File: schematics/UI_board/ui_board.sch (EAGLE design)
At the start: 119 parts, among them IC1 74HCT00N, IC10 74HCT32N, IC11 74HCT14N, IC12 74HCT14N, IC13 74HCT393N, IC2 74HCT151N, IC3 74HCT32N, IC4 74HCT74N, IC5 74HCT04N, IC6 74HCT32N, IC8 74HCT373N, IC9 74HCT32N

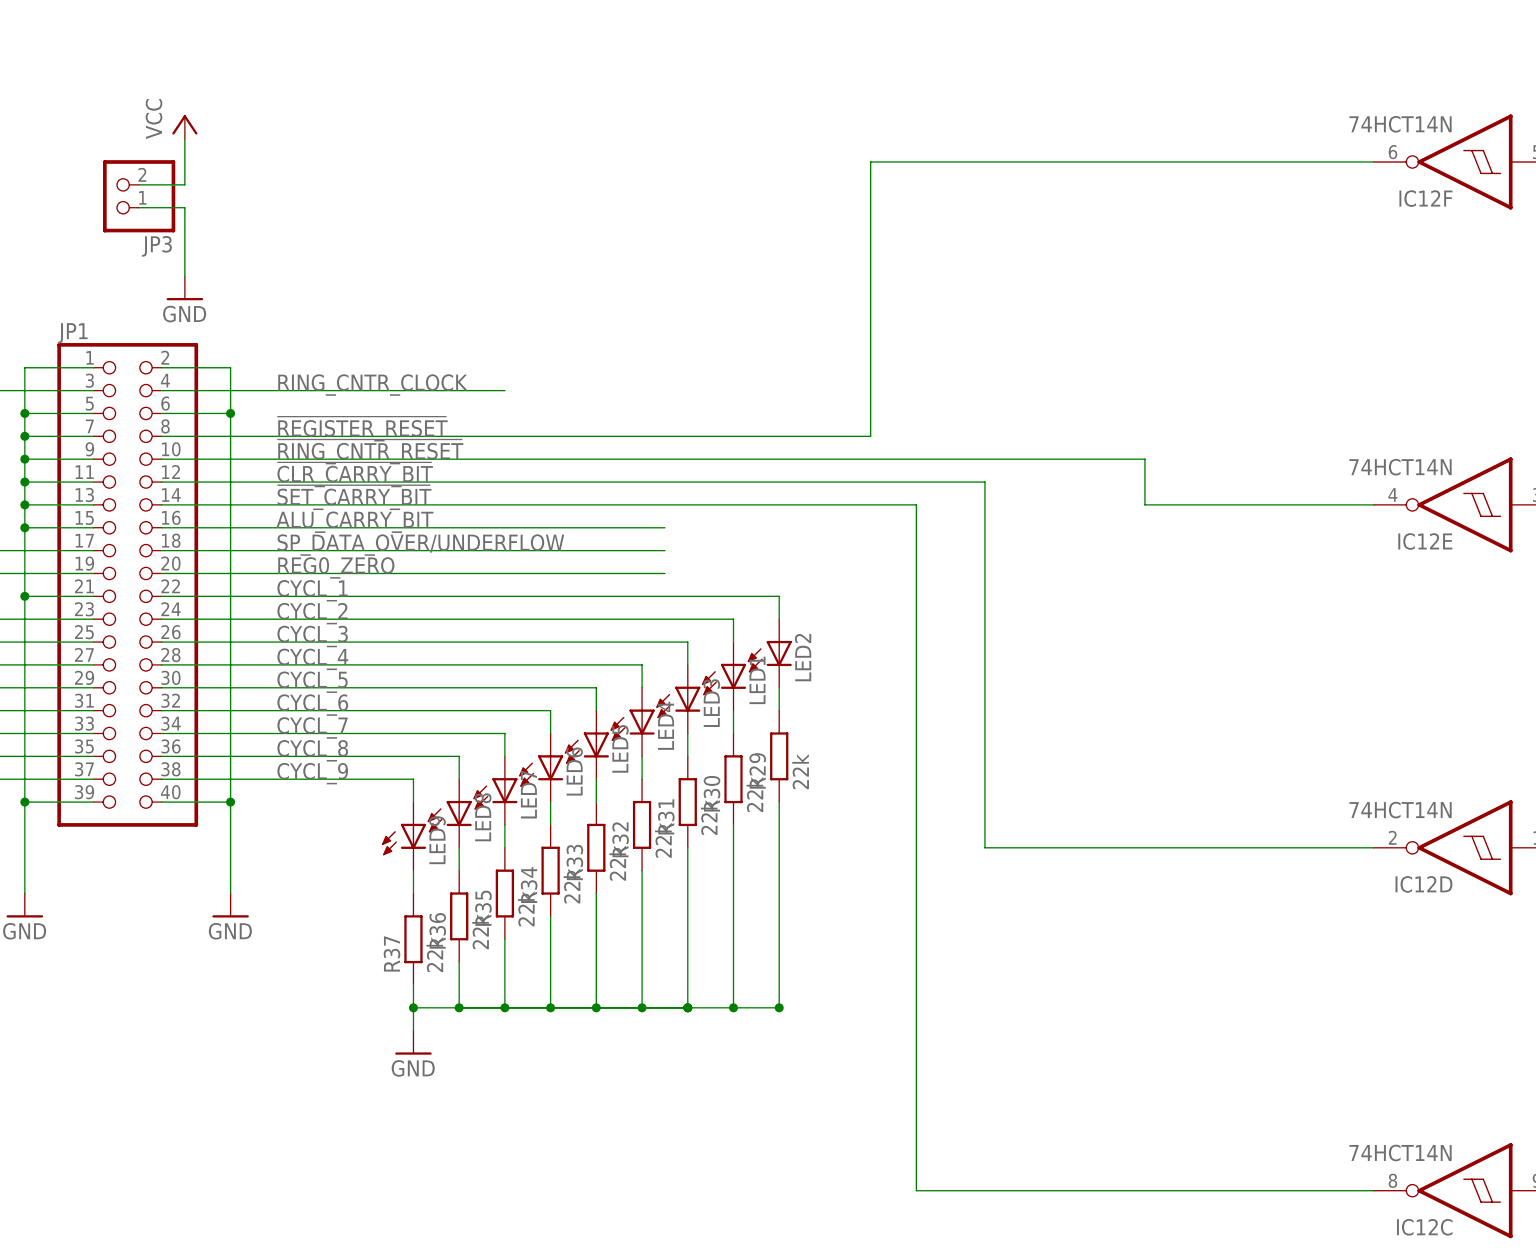
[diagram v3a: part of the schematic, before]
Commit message: got rid of two cycles! finetuning next
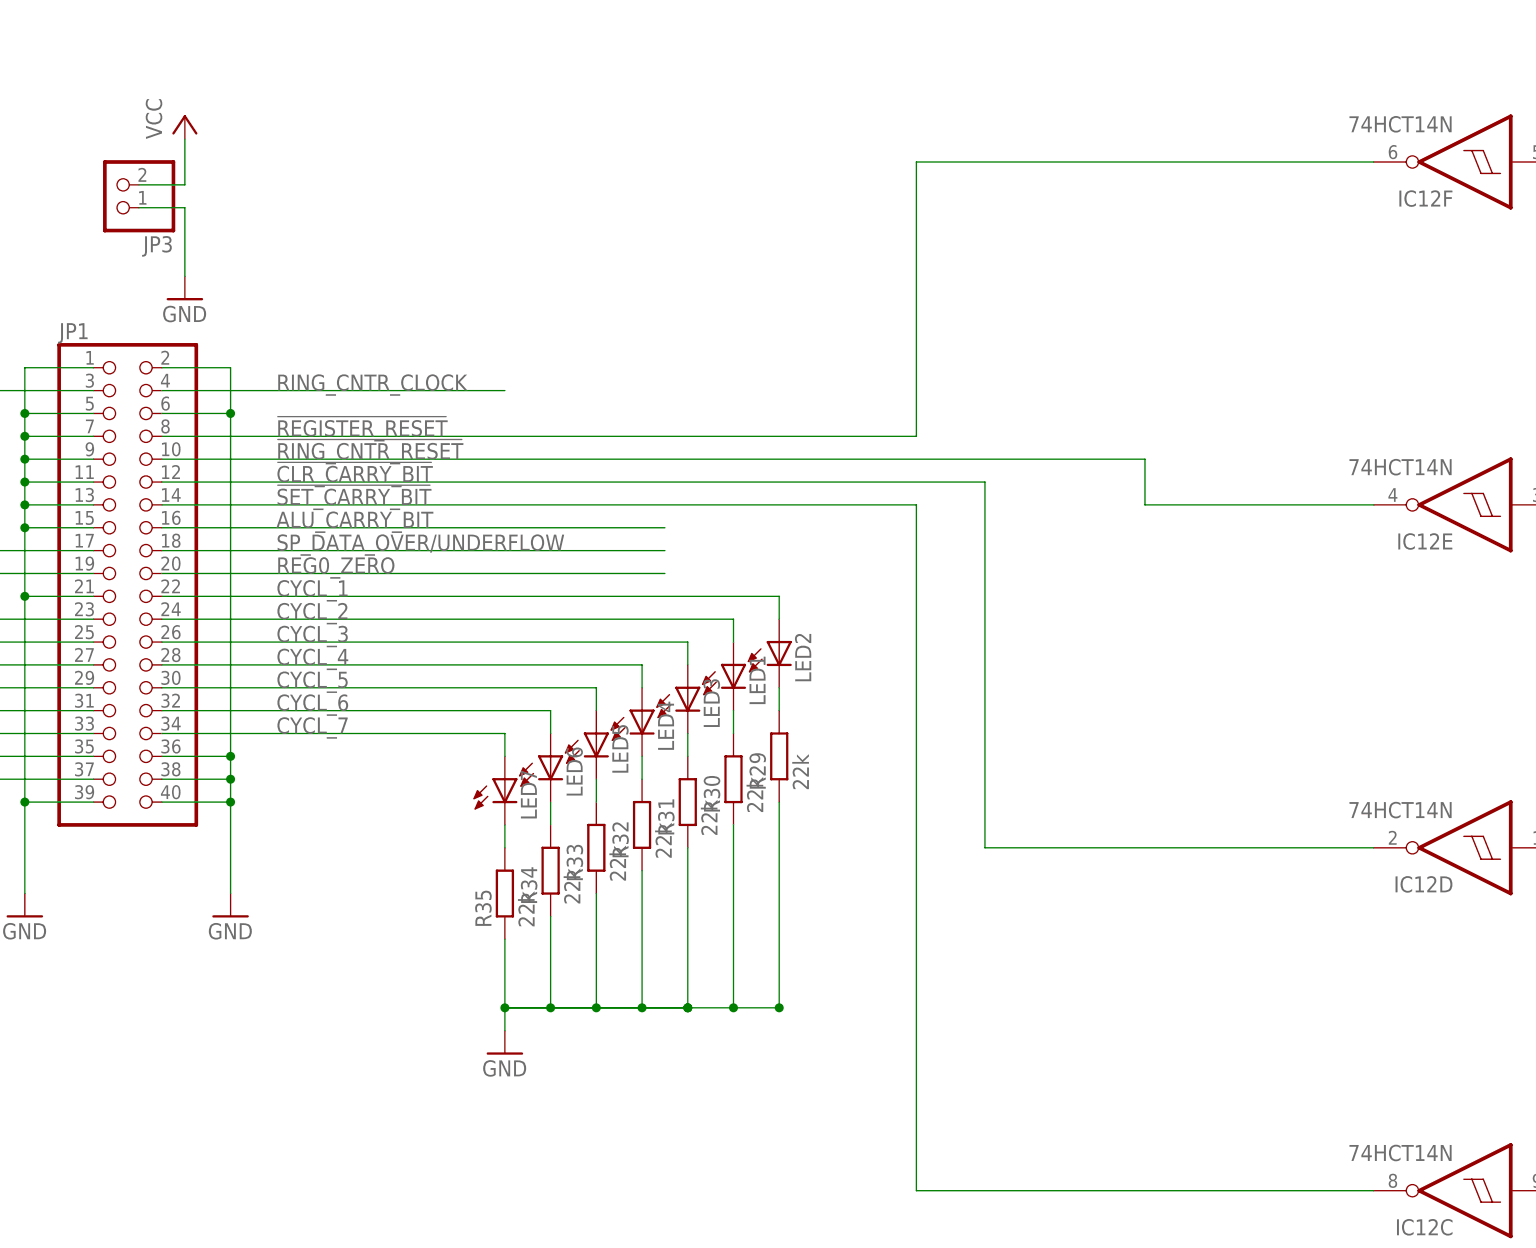
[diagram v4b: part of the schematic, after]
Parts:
- removed LED8, LED9: (no value), led:LED3MM
- removed R36, R37: 22k, rcl:R-EU_R1206
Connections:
- removed net CYCL_8: JP1.36, LED8.A
- removed net CYCL_9: JP1.38, LED9.A
- removed net N$67: LED8.C, R36.2
- removed net N$68: LED9.C, R37.2
- net GND: now also JP1.36, JP1.38; no longer R36.1, R37.1
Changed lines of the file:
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@@
 <part name="LED6" library="led" deviceset="LED" device="3MM"/>
 <part name="LED7" library="led" deviceset="LED" device="3MM"/>
-<part name="LED8" library="led" deviceset="LED" device="3MM"/>
-<part name="LED9" library="led" deviceset="LED" device="3MM"/>
 <part name="R29" library="rcl" deviceset="R-EU_" device="R1206" value="22k"/>
 <part name="R30" library="rcl" deviceset="R-EU_" device="R1206" value="22k"/>
@@
 <part name="R34" library="rcl" deviceset="R-EU_" device="R1206" value="22k"/>
 <part name="R35" library="rcl" deviceset="R-EU_" device="R1206" value="22k"/>
-<part name="R36" library="rcl" deviceset="R-EU_" device="R1206" value="22k"/>
-<part name="R37" library="rcl" deviceset="R-EU_" device="R1206" value="22k"/>
 <part name="GND32" library="supply1" deviceset="GND" device=""/>
 <part name="LED10" library="led" deviceset="LED" device="3MM"/>
@@
 <instance part="LED6" gate="G$1" x="58.42" y="40.64"/>
 <instance part="LED7" gate="G$1" x="53.34" y="38.1"/>
-<instance part="LED8" gate="G$1" x="48.26" y="35.56"/>
-<instance part="LED9" gate="G$1" x="43.18" y="33.02"/>
 <instance part="R29" gate="G$1" x="83.82" y="40.64" rot="R90"/>
 <instance part="R30" gate="G$1" x="78.74" y="38.1" rot="R90"/>
@@
 <instance part="R34" gate="G$1" x="58.42" y="27.94" rot="R90"/>
 <instance part="R35" gate="G$1" x="53.34" y="25.4" rot="R90"/>
-<instance part="R36" gate="G$1" x="48.26" y="22.86" rot="R90"/>
-<instance part="R37" gate="G$1" x="43.18" y="20.32" rot="R90"/>
-<instance part="GND32" gate="1" x="43.18" y="7.62"/>
+<instance part="GND32" gate="1" x="53.34" y="7.62"/>
 <instance part="LED10" gate="G$1" x="-66.04" y="50.8" rot="MR0"/>
 <instance part="LED12" gate="G$1" x="-60.96" y="48.26" rot="MR0"/>
@@
 <pinref part="JP1" gate="A" pin="8"/>
 <label x="27.94" y="76.2" size="1.778" layer="95"/>
-<wire x1="15.24" y1="76.2" x2="93.98" y2="76.2" width="0.1524" layer="91"/>
-<wire x1="93.98" y1="76.2" x2="93.98" y2="106.68" width="0.1524" layer="91"/>
-<wire x1="93.98" y1="106.68" x2="149.86" y2="106.68" width="0.1524" layer="91"/>
+<wire x1="15.24" y1="76.2" x2="99.06" y2="76.2" width="0.1524" layer="91"/>
+<wire x1="99.06" y1="76.2" x2="99.06" y2="106.68" width="0.1524" layer="91"/>
+<wire x1="99.06" y1="106.68" x2="149.86" y2="106.68" width="0.1524" layer="91"/>
 <pinref part="IC12" gate="F" pin="O"/>
 </segment>
@@
 <pinref part="LED7" gate="G$1" pin="A"/>
 <wire x1="53.34" y1="43.18" x2="53.34" y2="40.64" width="0.1524" layer="91"/>
-</segment>
-</net>
-<net name="CYCL_8" class="0">
-<segment>
-<pinref part="JP1" gate="A" pin="36"/>
-<wire x1="15.24" y1="40.64" x2="48.26" y2="40.64" width="0.1524" layer="91"/>
-<label x="27.94" y="40.64" size="1.778" layer="95"/>
-<pinref part="LED8" gate="G$1" pin="A"/>
-<wire x1="48.26" y1="38.1" x2="48.26" y2="40.64" width="0.1524" layer="91"/>
-</segment>
-</net>
-<net name="CYCL_9" class="0">
-<segment>
-<pinref part="JP1" gate="A" pin="38"/>
-<wire x1="15.24" y1="38.1" x2="43.18" y2="38.1" width="0.1524" layer="91"/>
-<label x="27.94" y="38.1" size="1.778" layer="95"/>
-<pinref part="LED9" gate="G$1" pin="A"/>
-<wire x1="43.18" y1="38.1" x2="43.18" y2="35.56" width="0.1524" layer="91"/>
 </segment>
 </net>
@@
 <wire x1="22.86" y1="83.82" x2="22.86" y2="78.74" width="0.1524" layer="91"/>
 <pinref part="JP1" gate="A" pin="6"/>
-<wire x1="22.86" y1="78.74" x2="22.86" y2="35.56" width="0.1524" layer="91"/>
+<wire x1="22.86" y1="78.74" x2="22.86" y2="40.64" width="0.1524" layer="91"/>
+<wire x1="22.86" y1="40.64" x2="22.86" y2="38.1" width="0.1524" layer="91"/>
+<wire x1="22.86" y1="38.1" x2="22.86" y2="35.56" width="0.1524" layer="91"/>
 <wire x1="22.86" y1="35.56" x2="22.86" y2="25.4" width="0.1524" layer="91"/>
 <wire x1="15.24" y1="78.74" x2="22.86" y2="78.74" width="0.1524" layer="91"/>
@@
 <junction x="22.86" y="78.74"/>
 <pinref part="GND2" gate="1" pin="GND"/>
+<pinref part="JP1" gate="A" pin="38"/>
+<wire x1="15.24" y1="38.1" x2="22.86" y2="38.1" width="0.1524" layer="91"/>
+<pinref part="JP1" gate="A" pin="36"/>
+<wire x1="15.24" y1="40.64" x2="22.86" y2="40.64" width="0.1524" layer="91"/>
+<junction x="22.86" y="38.1"/>
+<junction x="22.86" y="40.64"/>
 </segment>
 <segment>
@@
 <wire x1="-190.5" y1="-43.18" x2="-190.5" y2="-50.8" width="0.1524" layer="91"/>
 <pinref part="GND22" gate="1" pin="GND"/>
-</segment>
-<segment>
-<pinref part="GND32" gate="1" pin="GND"/>
-<wire x1="48.26" y1="12.7" x2="53.34" y2="12.7" width="0.1524" layer="91"/>
-<wire x1="53.34" y1="12.7" x2="58.42" y2="12.7" width="0.1524" layer="91"/>
-<wire x1="58.42" y1="12.7" x2="63.5" y2="12.7" width="0.1524" layer="91"/>
-<wire x1="63.5" y1="12.7" x2="68.58" y2="12.7" width="0.1524" layer="91"/>
-<wire x1="68.58" y1="12.7" x2="73.66" y2="12.7" width="0.1524" layer="91"/>
-<wire x1="83.82" y1="12.7" x2="78.74" y2="12.7" width="0.1524" layer="91"/>
-<pinref part="R36" gate="G$1" pin="1"/>
-<wire x1="78.74" y1="12.7" x2="73.66" y2="12.7" width="0.1524" layer="91"/>
-<wire x1="73.66" y1="12.7" x2="48.26" y2="12.7" width="0.1524" layer="91"/>
-<wire x1="48.26" y1="17.78" x2="48.26" y2="12.7" width="0.1524" layer="91"/>
-<pinref part="R35" gate="G$1" pin="1"/>
-<wire x1="53.34" y1="20.32" x2="53.34" y2="12.7" width="0.1524" layer="91"/>
-<pinref part="R34" gate="G$1" pin="1"/>
-<wire x1="58.42" y1="22.86" x2="58.42" y2="12.7" width="0.1524" layer="91"/>
-<pinref part="R33" gate="G$1" pin="1"/>
-<wire x1="63.5" y1="25.4" x2="63.5" y2="12.7" width="0.1524" layer="91"/>
-<pinref part="R32" gate="G$1" pin="1"/>
-<wire x1="68.58" y1="27.94" x2="68.58" y2="12.7" width="0.1524" layer="91"/>
-<pinref part="R31" gate="G$1" pin="1"/>
-<wire x1="73.66" y1="30.48" x2="73.66" y2="12.7" width="0.1524" layer="91"/>
-<pinref part="R30" gate="G$1" pin="1"/>
-<wire x1="78.74" y1="33.02" x2="78.74" y2="12.7" width="0.1524" layer="91"/>
-<pinref part="R29" gate="G$1" pin="1"/>
-<wire x1="83.82" y1="35.56" x2="83.82" y2="12.7" width="0.1524" layer="91"/>
-<junction x="83.82" y="12.7"/>
-<junction x="73.66" y="12.7"/>
-<junction x="78.74" y="12.7"/>
-<junction x="73.66" y="12.7"/>
-<junction x="68.58" y="12.7"/>
-<junction x="63.5" y="12.7"/>
-<junction x="58.42" y="12.7"/>
-<junction x="53.34" y="12.7"/>
-<pinref part="R37" gate="G$1" pin="1"/>
-<wire x1="43.18" y1="15.24" x2="43.18" y2="12.7" width="0.1524" layer="91"/>
-<junction x="48.26" y="12.7"/>
-<wire x1="43.18" y1="12.7" x2="43.18" y2="10.16" width="0.1524" layer="91"/>
-<wire x1="48.26" y1="12.7" x2="43.18" y2="12.7" width="0.1524" layer="91"/>
-<junction x="43.18" y="12.7"/>
 </segment>
 <segment>
@@
 <wire x1="165.1" y1="-66.04" x2="165.1" y2="-68.58" width="0.1524" layer="91"/>
 </segment>
+<segment>
+<wire x1="53.34" y1="12.7" x2="58.42" y2="12.7" width="0.1524" layer="91"/>
+<wire x1="58.42" y1="12.7" x2="63.5" y2="12.7" width="0.1524" layer="91"/>
+<wire x1="63.5" y1="12.7" x2="68.58" y2="12.7" width="0.1524" layer="91"/>
+<wire x1="68.58" y1="12.7" x2="73.66" y2="12.7" width="0.1524" layer="91"/>
+<wire x1="83.82" y1="12.7" x2="78.74" y2="12.7" width="0.1524" layer="91"/>
+<wire x1="78.74" y1="12.7" x2="73.66" y2="12.7" width="0.1524" layer="91"/>
+<wire x1="73.66" y1="12.7" x2="53.34" y2="12.7" width="0.1524" layer="91"/>
+<pinref part="R35" gate="G$1" pin="1"/>
+<wire x1="53.34" y1="20.32" x2="53.34" y2="12.7" width="0.1524" layer="91"/>
+<pinref part="R34" gate="G$1" pin="1"/>
+<wire x1="58.42" y1="22.86" x2="58.42" y2="12.7" width="0.1524" layer="91"/>
+<pinref part="R33" gate="G$1" pin="1"/>
+<wire x1="63.5" y1="25.4" x2="63.5" y2="12.7" width="0.1524" layer="91"/>
+<pinref part="R32" gate="G$1" pin="1"/>
+<wire x1="68.58" y1="27.94" x2="68.58" y2="12.7" width="0.1524" layer="91"/>
+<pinref part="R31" gate="G$1" pin="1"/>
+<wire x1="73.66" y1="30.48" x2="73.66" y2="12.7" width="0.1524" layer="91"/>
+<pinref part="R30" gate="G$1" pin="1"/>
+<wire x1="78.74" y1="33.02" x2="78.74" y2="12.7" width="0.1524" layer="91"/>
+<pinref part="R29" gate="G$1" pin="1"/>
+<wire x1="83.82" y1="35.56" x2="83.82" y2="12.7" width="0.1524" layer="91"/>
+<junction x="83.82" y="12.7"/>
+<junction x="73.66" y="12.7"/>
+<junction x="78.74" y="12.7"/>
+<junction x="73.66" y="12.7"/>
+<junction x="68.58" y="12.7"/>
+<junction x="63.5" y="12.7"/>
+<junction x="58.42" y="12.7"/>
+<junction x="53.34" y="12.7"/>
+<pinref part="GND32" gate="1" pin="GND"/>
+<wire x1="53.34" y1="10.16" x2="53.34" y2="12.7" width="0.1524" layer="91"/>
+</segment>
 </net>
 <net name="SINGLE_STEP_CLOCK" class="0">
@@
 </segment>
 </net>
-<net name="N$67" class="0">
-<segment>
-<pinref part="LED8" gate="G$1" pin="C"/>
-<pinref part="R36" gate="G$1" pin="2"/>
-<wire x1="48.26" y1="30.48" x2="48.26" y2="27.94" width="0.1524" layer="91"/>
-</segment>
-</net>
-<net name="N$68" class="0">
-<segment>
-<pinref part="LED9" gate="G$1" pin="C"/>
-<pinref part="R37" gate="G$1" pin="2"/>
-<wire x1="43.18" y1="27.94" x2="43.18" y2="25.4" width="0.1524" layer="91"/>
-</segment>
-</net>

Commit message: soldered ui bord
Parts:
- removed R2: (no value), rcl:R-EU_R1206
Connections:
- removed net N$3: IC1C.I1, R2.1, S1.S1
- net GND: now also IC10A.I0, IC10A.I1, IC5B.I, IC5C.I, IC5D.I, IC5E.I
- net N$5: now also IC1C.I1, S1.S1
- net VCC: no longer R2.2
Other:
- moved on the sheet: C1, C10, C11, C12, IC12C, IC12D, IC12E, IC12F, R21, R22, R23, R24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
